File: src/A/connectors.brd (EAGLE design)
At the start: 36 x 14.4 mm, 11 parts, among them CON1 CON-4P-TABS-JST_GH-RA, CON2 CON-4P-TABS-JST_GH-RA, CON3 PINHEAD_1X04-2, CON4 PINHEAD_1X04-2, IC6 TJA1051-HVSON8, IC8 TPD3S014DBVR-SOT23-6

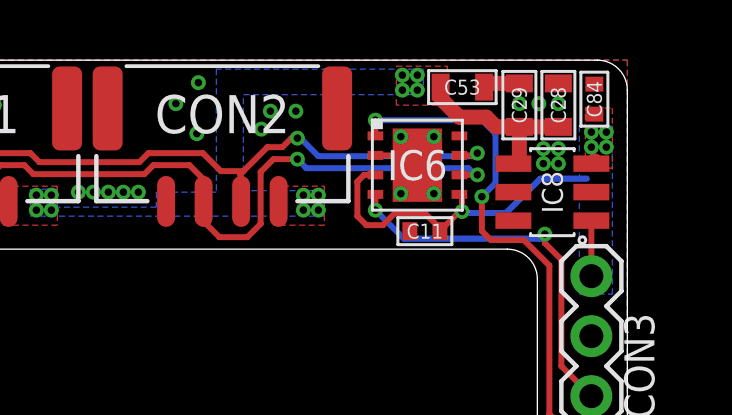
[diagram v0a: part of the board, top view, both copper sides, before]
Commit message: rearrangement and alternate power stage design added
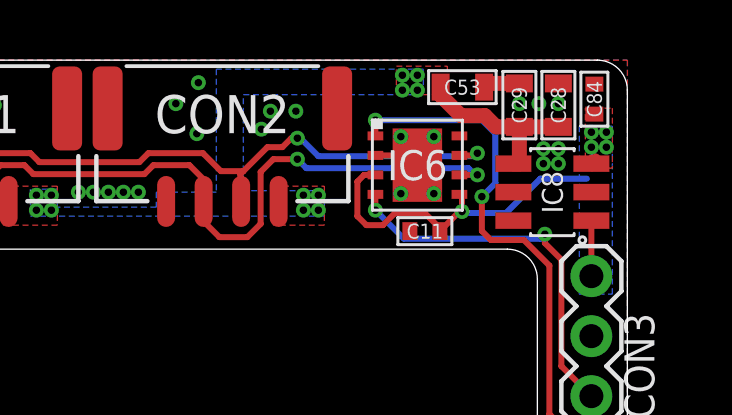
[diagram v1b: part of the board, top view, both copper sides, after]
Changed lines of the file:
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@@
 </layers>
 <board>
-<fusionsync huburn="a.cGVyc29uYWw6dWUyYWE4ZDY4" projecturn="a.cGVyc29uYWw6dWUyYWE4ZDY4IzIwMjAwOTI1MzM2NDYxMjgx" f3durn="urn:adsk.wipprod:dm.lineage:5f-RR5beSAqgs6k1iF_brA" pcbguid="" lastpulledtime="" lastsyncedchangeguid="" latestrevisionid="91c3f639-02cc-4b84-a14b-e3aaad1c6eab" lastsyncedrevisionid="91c3f639-02cc-4b84-a14b-e3aaad1c6eab" lastboardhashguid="354a8440-501e-4556-71f2-56a415103d28" lastpushedtime="2020-10-31T23:22:11Z" linktopcb3d="true"/>
+<fusionsync huburn="a.cGVyc29uYWw6dWUyYWE4ZDY4" projecturn="a.cGVyc29uYWw6dWUyYWE4ZDY4IzIwMjAwOTI1MzM2NDYxMjgx" f3durn="urn:adsk.wipprod:dm.lineage:5f-RR5beSAqgs6k1iF_brA" pcbguid="" lastpulledtime="" lastsyncedchangeguid="" latestrevisionid="04173ad2-e432-4cf5-9b9d-9b2dc3d49b22" lastsyncedrevisionid="04173ad2-e432-4cf5-9b9d-9b2dc3d49b22" lastboardhashguid="f24dbab6-befe-c805-d208-4619c0b274fc" lastpushedtime="2020-11-10T14:33:02Z" linktopcb3d="true"/>
 <plain>
 <wire x1="5.5" y1="75.1" x2="5.5" y2="74.1" width="0.1524" layer="138"/>
@@
 </polygon>
 <polygon width="0.2" layer="1" thermals="no">
-<vertex x="12" y="78.5"/>
-<vertex x="10.3" y="78.5"/>
+<vertex x="12" y="78.85"/>
+<vertex x="10.3" y="78.85"/>
 <vertex x="10.3" y="79.8"/>
 <vertex x="12" y="79.8"/>
@@
 <wire x1="14.4" y1="76.55" x2="14.2" y2="76.55" width="0.5" layer="1"/>
 <wire x1="14.4" y1="77.775" x2="13.625" y2="77.775" width="0.5" layer="1"/>
-<wire x1="13.625" y1="77.775" x2="13.3" y2="78.1" width="0.5" layer="1"/>
-<wire x1="13.3" y1="78.1" x2="12.4" y2="78.1" width="0.5" layer="1"/>
-<wire x1="12.4" y1="78.1" x2="11.775" y2="78.725" width="0.5" layer="1"/>
-<wire x1="11.775" y1="78.725" x2="11.775" y2="79.1" width="0.5" layer="1"/>
+<wire x1="13.625" y1="77.775" x2="13.25" y2="78.15" width="0.5" layer="1"/>
+<wire x1="13.25" y1="78.15" x2="12.45" y2="78.15" width="0.5" layer="1"/>
+<wire x1="12.45" y1="78.15" x2="11.775" y2="78.825" width="0.5" layer="1"/>
+<wire x1="11.775" y1="78.825" x2="11.775" y2="79.1" width="0.5" layer="1"/>
 </signal>
 </signals>

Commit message: variant A updates
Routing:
- net N$23: track 22.2 -> 20.9 mm
- net N$25: track 26.5 -> 25.8 mm
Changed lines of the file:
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@@
 <via x="13" y="76.9" extent="1-16" drill="0.25" diameter="0.5"/>
 <wire x1="-3.875" y1="75.29" x2="-3.875" y2="76.125" width="0.2" layer="1"/>
-<wire x1="5.125" y1="74.725" x2="5.125" y2="75.29" width="0.2" layer="1"/>
-<wire x1="5.125" y1="75.29" x2="5.125" y2="75.825" width="0.2" layer="1"/>
-<wire x1="6.8" y1="77.4" x2="7" y2="77.4" width="0.2" layer="1"/>
-<wire x1="6.8" y1="77.4" x2="6.5" y2="77.1" width="0.2" layer="1"/>
-<wire x1="6.5" y1="77.1" x2="6" y2="77.1" width="0.2" layer="1"/>
+<wire x1="7" y1="77.4" x2="6.8" y2="77.4" width="0.2" layer="1"/>
 <via x="7" y="77.4" extent="1-16" drill="0.25" diameter="0.5"/>
 <wire x1="-3.875" y1="76.125" x2="-3.1" y2="76.9" width="0.2" layer="1"/>
@@
 <wire x1="-1.6" y1="76.6" x2="1.7343125" y2="76.6" width="0.2" layer="1"/>
 <wire x1="1.7343125" y1="76.6" x2="2.0343125" y2="76.9" width="0.2" layer="1"/>
-<wire x1="5.075" y1="75.875" x2="5.125" y2="75.825" width="0.2" layer="1"/>
 <wire x1="2.0343125" y1="76.9" x2="3.85" y2="76.9" width="0.2" layer="1"/>
-<wire x1="3.85" y1="76.9" x2="4.45" y2="76.3" width="0.2" layer="1"/>
 <wire x1="5.125" y1="75.29" x2="5.1" y2="75.315" width="0.2" layer="1"/>
-<wire x1="5.1" y1="76.2" x2="5.1" y2="75.315" width="0.2" layer="1"/>
-<wire x1="6" y1="77.1" x2="5.2" y2="76.3" width="0.2" layer="1"/>
-<wire x1="5.2" y1="76.3" x2="5.1" y2="76.2" width="0.2" layer="1"/>
-<wire x1="4.45" y1="76.3" x2="5.2" y2="76.3" width="0.2" layer="1"/>
+<wire x1="5.1" y1="75.95" x2="5.1" y2="75.315" width="0.2" layer="1"/>
 <wire x1="7" y1="77.4" x2="7.1" y2="77.4" width="0.2" layer="16"/>
 <wire x1="7.1" y1="77.4" x2="7.7" y2="76.8" width="0.2" layer="16"/>
 <wire x1="13" y1="76.9" x2="12.9" y2="76.8" width="0.2" layer="16"/>
 <wire x1="12.9" y1="76.8" x2="7.7" y2="76.8" width="0.2" layer="16"/>
+<wire x1="4.8" y1="75.95" x2="5.1" y2="75.95" width="0.2" layer="1"/>
+<wire x1="5.155025" y1="75.95" x2="5.1" y2="75.95" width="0.2" layer="1"/>
+<wire x1="3.85" y1="76.9" x2="4.8" y2="75.95" width="0.2" layer="1"/>
+<wire x1="6.45" y1="77.05" x2="6.255025" y2="77.05" width="0.2" layer="1"/>
+<wire x1="6.8" y1="77.4" x2="6.45" y2="77.05" width="0.2" layer="1"/>
+<wire x1="6.255025" y1="77.05" x2="5.155025" y2="75.95" width="0.2" layer="1"/>
 </signal>
 <signal name="N$25">
@@
 <wire x1="12.4" y1="76.175" x2="13" y2="76.175" width="0.2" layer="1"/>
 <via x="13" y="76.175" extent="1-16" drill="0.25" diameter="0.5"/>
-<wire x1="-5.125" y1="75.29" x2="-5.125" y2="75.775" width="0.2" layer="1"/>
 <wire x1="3.875" y1="76.025" x2="3.875" y2="75.29" width="0.2" layer="1"/>
 <via x="7" y="76.7" extent="1-16" drill="0.25" diameter="0.5"/>
@@
 <wire x1="3.875" y1="74.625" x2="4.4" y2="74.1" width="0.2" layer="1"/>
 <wire x1="4.4" y1="74.1" x2="5.33353125" y2="74.1" width="0.2" layer="1"/>
-<wire x1="6.2" y1="76.7" x2="7" y2="76.7" width="0.2" layer="1"/>
-<wire x1="5.775" y1="74.54146875" x2="5.775" y2="76.275" width="0.2" layer="1"/>
-<wire x1="5.775" y1="76.275" x2="6.2" y2="76.7" width="0.2" layer="1"/>
+<wire x1="6.45" y1="76.7" x2="7" y2="76.7" width="0.2" layer="1"/>
+<wire x1="5.775" y1="74.54146875" x2="5.775" y2="76.025" width="0.2" layer="1"/>
+<wire x1="5.775" y1="76.025" x2="6.45" y2="76.7" width="0.2" layer="1"/>
 <wire x1="12.925" y1="76.175" x2="12.7" y2="76.4" width="0.2" layer="16"/>
 <wire x1="12.925" y1="76.175" x2="13" y2="76.175" width="0.2" layer="16"/>
@@
 <via x="-1.7" y="75.5" extent="1-16" drill="0.25" diameter="0.5"/>
 <via x="7.2" y="75.5" extent="1-16" drill="0.25" diameter="0.5"/>
-<wire x1="6.375" y1="74.9" x2="6.375" y2="75.29" width="0.5" layer="1"/>
 <via x="-1.2" y="75.5" extent="1-16" drill="0.25" diameter="0.5"/>
 <via x="-1.7" y="75" extent="1-16" drill="0.25" diameter="0.5"/>
